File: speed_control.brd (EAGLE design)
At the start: 160 x 100 mm, 3 parts

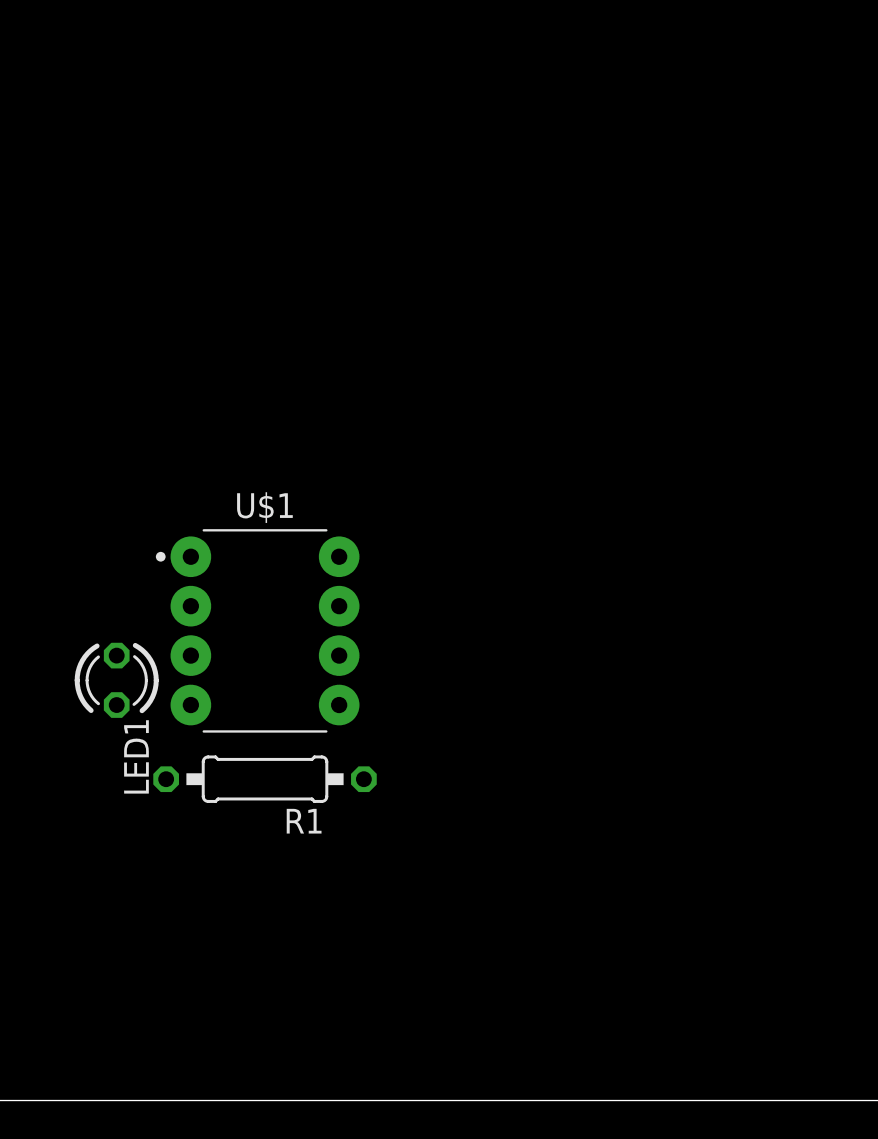
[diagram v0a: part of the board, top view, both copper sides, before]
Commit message: Added headers to circuit
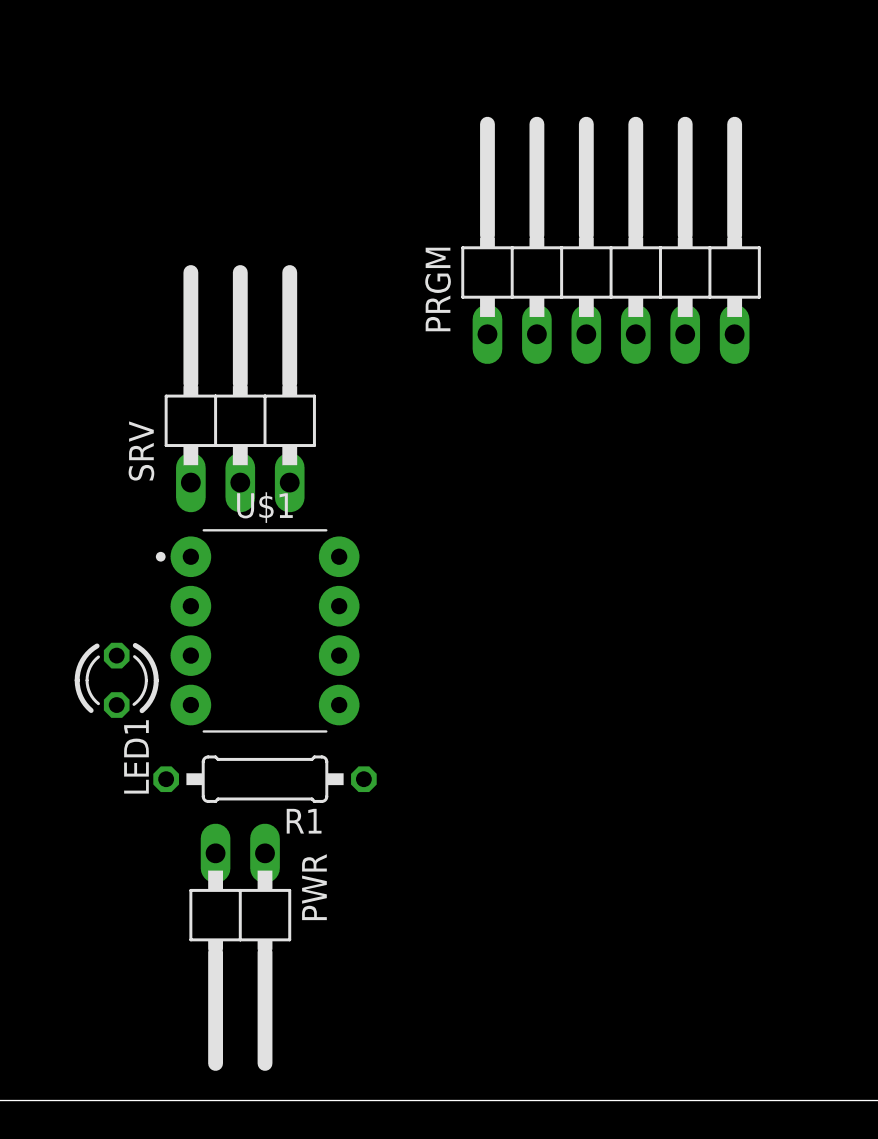
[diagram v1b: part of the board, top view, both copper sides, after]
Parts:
- added PRGM: (no value), pinhead:1X06/90
- added PWR: (no value), pinhead:1X02/90
- added SRV: (no value), pinhead:1X03/90
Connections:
- new net MCLR/VPP: PRGM.1
- new net PGC/ICSPCLK: PRGM.5
- new net PGD/ICSPDAT: PRGM.4
- new net PGM/LVP: PRGM.6
- new net VDD: PRGM.2
- new net VSS: PRGM.3
- net 5V: now also PWR.1, SRV.2
- net GND: now also PWR.2, SRV.1
- net SIGNAL: now also SRV.3
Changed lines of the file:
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@@
 </autorouter>
 <elements>
-<element name="U$1" library="PIC10F222" package="DIP762W53P254L955H330Q8B" package3d_urn="urn:adsk.eagle:package:16702925/1" value="PIC10F222PIC10F222" x="22.86" y="24.13" smashed="yes">
-<attribute name="NAME" x="22.86" y="29.9329" size="1.27" layer="25" align="bottom-center"/>
-<attribute name="VALUE" x="22.86" y="18.3271" size="1.27" layer="27" align="top-center"/>
-</element>
 <element name="LED1" library="led" library_urn="urn:adsk.eagle:library:259" package="LED3MM" package3d_urn="urn:adsk.eagle:package:15797/1" value="" x="15.24" y="21.59" smashed="yes" rot="R270">
 <attribute name="NAME" x="15.621" y="19.685" size="1.27" layer="25" ratio="10" rot="R270"/>
@@
 <attribute name="VALUE" x="25.1206" y="17.145" size="1.27" layer="27" ratio="10" rot="R180"/>
 </element>
+<element name="SRV" library="pinhead" library_urn="urn:adsk.eagle:library:325" package="1X03/90" package3d_urn="urn:adsk.eagle:package:22459/2" value="" x="21.59" y="35.56" smashed="yes">
+<attribute name="NAME" x="17.145" y="31.75" size="1.27" layer="25" ratio="10" rot="R90"/>
+<attribute name="POPULARITY" value="17" x="21.59" y="35.56" size="1.778" layer="27" display="off"/>
+<attribute name="VALUE" x="27.305" y="31.75" size="1.27" layer="27" rot="R90"/>
+</element>
+<element name="PWR" library="pinhead" library_urn="urn:adsk.eagle:library:325" package="1X02/90" package3d_urn="urn:adsk.eagle:package:22437/2" value="" x="21.59" y="8.89" smashed="yes" rot="R180">
+<attribute name="NAME" x="24.765" y="12.7" size="1.27" layer="25" ratio="10" rot="R270"/>
+<attribute name="POPULARITY" value="24" x="21.59" y="8.89" size="1.778" layer="27" rot="R180" display="off"/>
+<attribute name="VALUE" x="17.145" y="12.7" size="1.27" layer="27" rot="R270"/>
+</element>
+<element name="PRGM" library="pinhead" library_urn="urn:adsk.eagle:library:325" package="1X06/90" package3d_urn="urn:adsk.eagle:package:22475/2" value="" x="40.64" y="43.18" smashed="yes">
+<attribute name="NAME" x="32.385" y="39.37" size="1.27" layer="25" ratio="10" rot="R90"/>
+<attribute name="POPULARITY" value="10" x="40.64" y="43.18" size="1.778" layer="27" display="off"/>
+<attribute name="VALUE" x="50.165" y="39.37" size="1.27" layer="27" rot="R90"/>
+</element>
+<element name="U$1" library="PIC10F222" package="DIP762W53P254L955H330Q8B" package3d_urn="urn:adsk.eagle:package:16702925/1" value="PIC10F222PIC10F222" x="22.86" y="24.13" smashed="yes">
+<attribute name="NAME" x="22.86" y="29.9329" size="1.27" layer="25" align="bottom-center"/>
+<attribute name="VALUE" x="22.86" y="18.3271" size="1.27" layer="27" align="top-center"/>
+</element>
 </elements>
 <signals>
 <signal name="GND">
+<contactref element="R1" pad="1"/>
+<contactref element="PWR" pad="2"/>
+<contactref element="SRV" pad="1"/>
 <contactref element="U$1" pad="7"/>
-<contactref element="R1" pad="1"/>
-<wire x1="26.67" y1="25.4" x2="27.94" y2="16.51" width="0" layer="19" extent="1-1"/>
+<wire x1="27.94" y1="16.51" x2="26.67" y2="25.4" width="0" layer="19" extent="1-1"/>
+<wire x1="20.32" y1="12.7" x2="27.94" y2="16.51" width="0" layer="19" extent="1-1"/>
+<wire x1="19.05" y1="31.75" x2="26.67" y2="25.4" width="0" layer="19" extent="1-1"/>
 </signal>
 <signal name="5V">
+<contactref element="PWR" pad="1"/>
+<contactref element="SRV" pad="2"/>
 <contactref element="U$1" pad="2"/>
-</signal>
-<signal name="POT">
-<contactref element="U$1" pad="5"/>
+<wire x1="19.05" y1="25.4" x2="21.59" y2="31.75" width="0" layer="19" extent="1-1"/>
+<wire x1="22.86" y1="12.7" x2="19.05" y2="25.4" width="0" layer="19" extent="1-1"/>
 </signal>
 <signal name="SIGNAL">
+<contactref element="SRV" pad="3"/>
 <contactref element="U$1" pad="4"/>
+<wire x1="19.05" y1="20.32" x2="24.13" y2="31.75" width="0" layer="19" extent="1-1"/>
 </signal>
 <signal name="N$1">
+<contactref element="LED1" pad="A"/>
 <contactref element="U$1" pad="3"/>
-<contactref element="LED1" pad="A"/>
-<wire x1="19.05" y1="22.86" x2="15.24" y2="22.86" width="0" layer="19" extent="1-1"/>
+<wire x1="15.24" y1="22.86" x2="19.05" y2="22.86" width="0" layer="19" extent="1-1"/>
 </signal>
 <signal name="N$2">
@@
 <wire x1="17.78" y1="16.51" x2="15.24" y2="20.32" width="0" layer="19" extent="1-1"/>
 </signal>
+<signal name="MCLR/VPP">
+<contactref element="PRGM" pad="1"/>
+</signal>
+<signal name="VDD">
+<contactref element="PRGM" pad="2"/>
+</signal>
+<signal name="VSS">
+<contactref element="PRGM" pad="3"/>
+</signal>
+<signal name="PGD/ICSPDAT">
+<contactref element="PRGM" pad="4"/>
+</signal>
+<signal name="PGC/ICSPCLK">
+<contactref element="PRGM" pad="5"/>
+</signal>
+<signal name="PGM/LVP">
+<contactref element="PRGM" pad="6"/>
+</signal>
+<signal name="POT">
+<contactref element="U$1" pad="5"/>
+</signal>
 </signals>

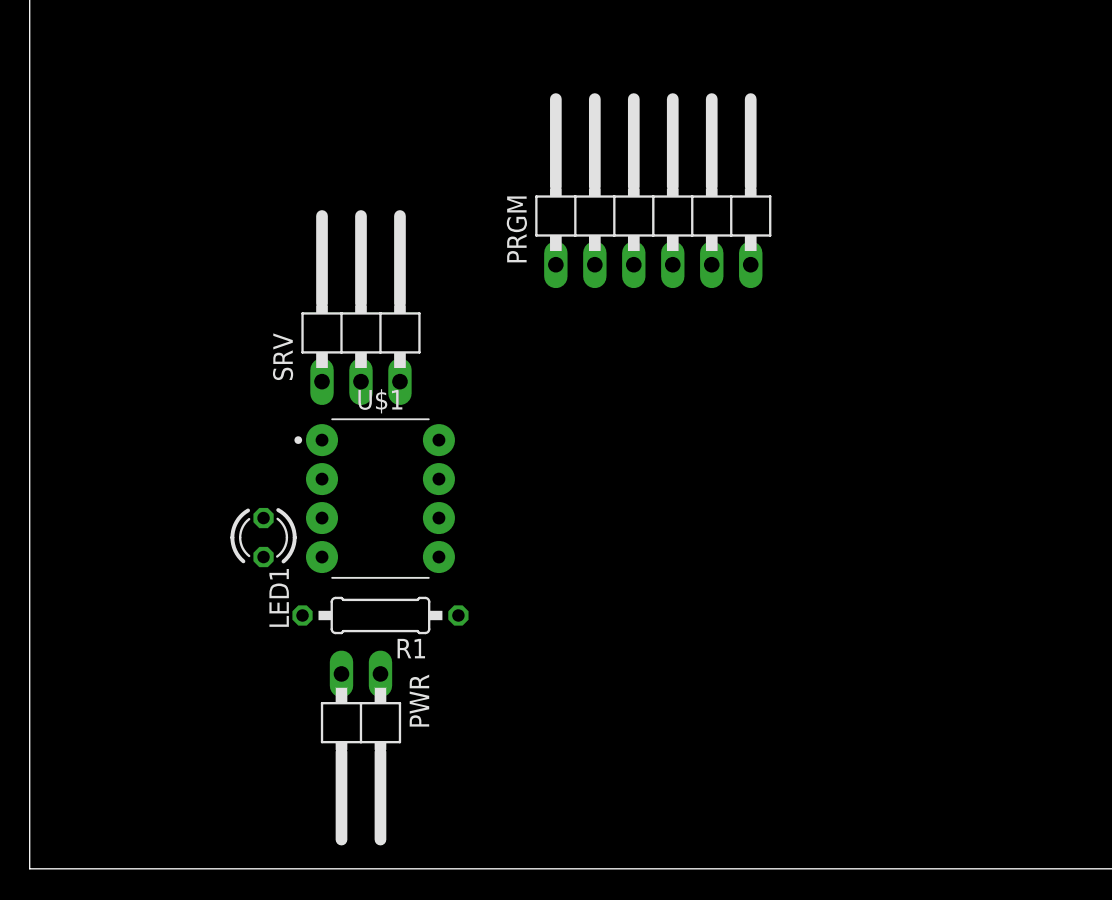
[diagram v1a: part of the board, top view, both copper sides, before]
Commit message: Added programming interface
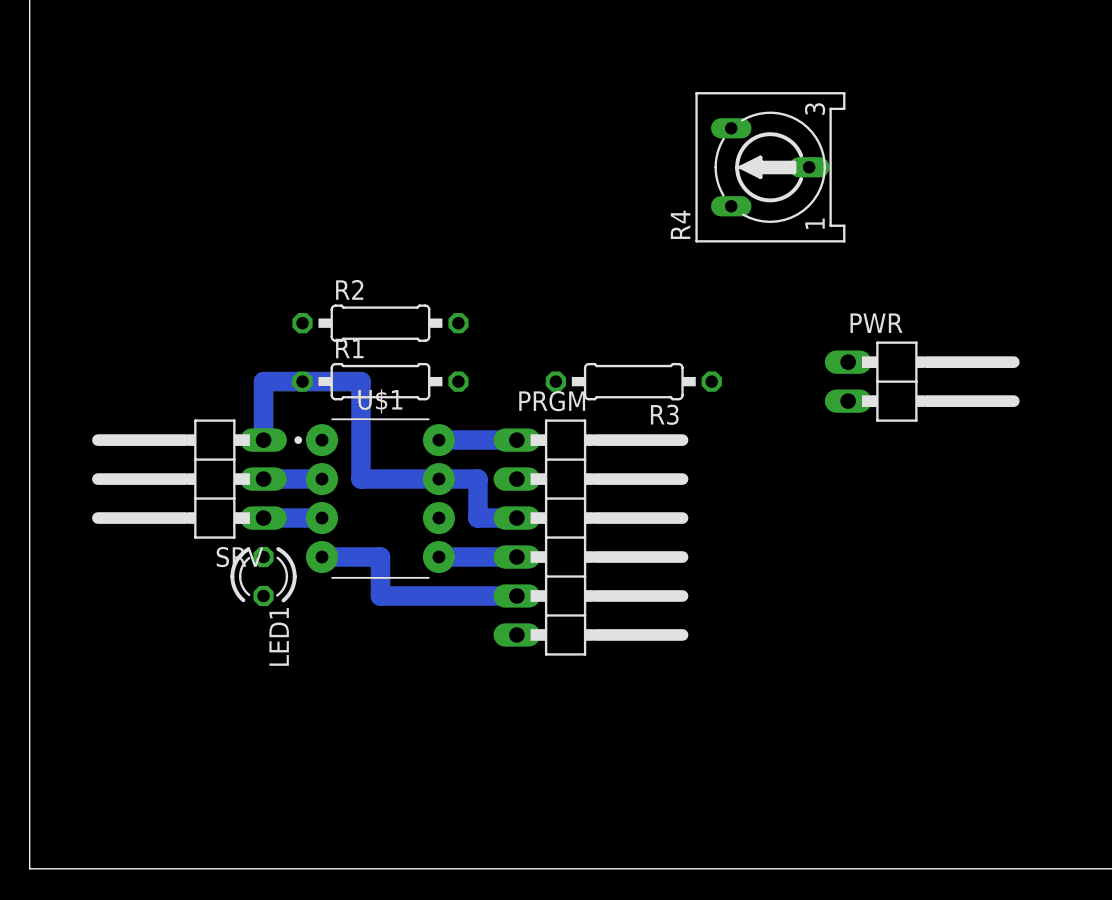
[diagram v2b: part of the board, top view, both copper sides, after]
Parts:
- added R2, R3: 1k, rcl:0207/10
- added R4: (no value), pot:RS3
- R1: value (none) -> 270
- moved PWR 42.3 mm to (57.1, 31.8), turned to 270 degrees
- moved PRGM 22.2 mm to (35.6, 21.6), turned to 270 degrees
- moved R1 15.2 mm to (22.9, 31.8), turned to 0 degrees
- moved SRV 14.4 mm to (11.4, 25.4), turned to 90 degrees
- moved LED1 2.54 mm to (15.2, 19.1)
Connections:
- removed net POT: U$1.5
- removed net VDD: PRGM.2
- removed net VSS: PRGM.3
- net 5V: now also PRGM.2, PWR.2, R2.1, R4.E; no longer PWR.1
- net GND: now also PRGM.3, PWR.1, R4.A, SRV.3; no longer PWR.2, SRV.1
- net MCLR/VPP: now also R2.2, U$1.8
- net N$1: now also R3.2, R4.S; no longer LED1.A, U$1.3
- net PGC/ICSPCLK: now also LED1.A, U$1.4
- net PGD/ICSPDAT: now also R3.1, U$1.5
- net SIGNAL: now also SRV.1, U$1.3; no longer SRV.3, U$1.4
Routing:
- net GND: track 0.00 -> 29.2 mm
- net PGC/ICSPCLK: track 0.00 -> 15.2 mm
- net PGD/ICSPDAT: track 0.00 -> 5.08 mm
- net MCLR/VPP: track 0.00 -> 5.08 mm
- net SIGNAL: track 0.00 -> 3.81 mm
- net 5V: track 0.00 -> 3.81 mm

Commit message: Layout of PCB complete
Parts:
- removed R4: (no value), pot:RS3
- added POT: (no value), pinhead:1X03
- PRGM: device pinhead:1X06/90 -> pinhead:1X06
- R2: value 1k -> 10k
- moved PWR 56.8 mm to (1.27, 21.6), turned to 90 degrees
- moved R3 26.9 mm to (20.3, 12.7), turned to 90 degrees
- moved R2 25.9 mm to (27.9, 10.2), turned to 90 degrees
- moved R1 24.4 mm to (7.62, 12.7), turned to 270 degrees
- moved PRGM 17.1 mm to (24.1, 8.89)
- moved LED1 16.5 mm to (8.89, 3.81), turned to 180 degrees
- moved SRV 16.3 mm to (1.27, 12.7)
- moved U$1 15.5 mm to (14.0, 11.4)
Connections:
- net 5V: now also POT.3; no longer R4.E
- net GND: now also POT.1; no longer R4.A
- net N$1: now also POT.2; no longer R4.S
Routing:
- net 5V: track 3.81 -> 109.8 mm
- net GND: track 29.2 -> 93.6 mm
- net PGC/ICSPCLK: track 15.2 -> 33.3 mm
- net MCLR/VPP: track 5.08 -> 10.2 mm
- net N$2: track 0.00 -> 3.81 mm
- net N$1: track 0.00 -> 2.54 mm
- net SIGNAL: track 3.81 -> 5.08 mm
- net PGD/ICSPDAT: track 5.08 -> 6.35 mm
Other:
- board size 160 x 100 mm -> 31.7 x 23.8 mm

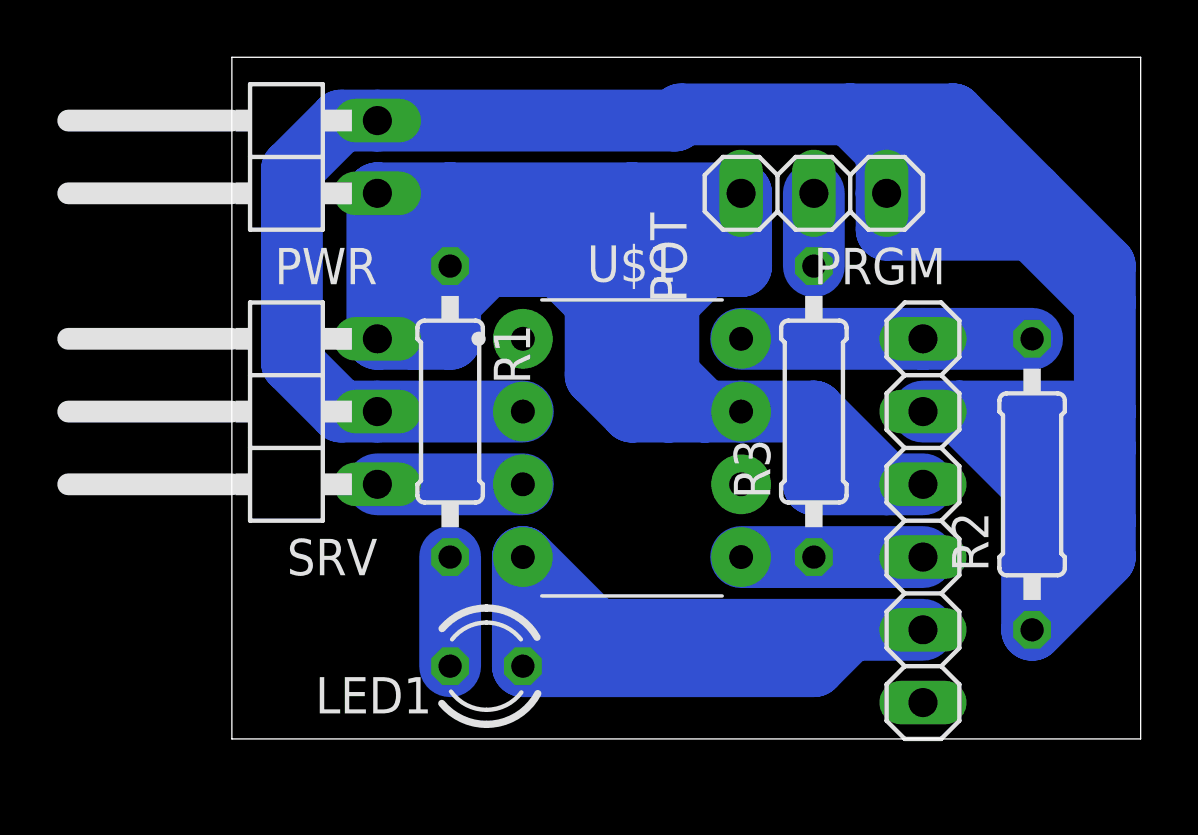
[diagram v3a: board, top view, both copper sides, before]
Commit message: Moved board to origin
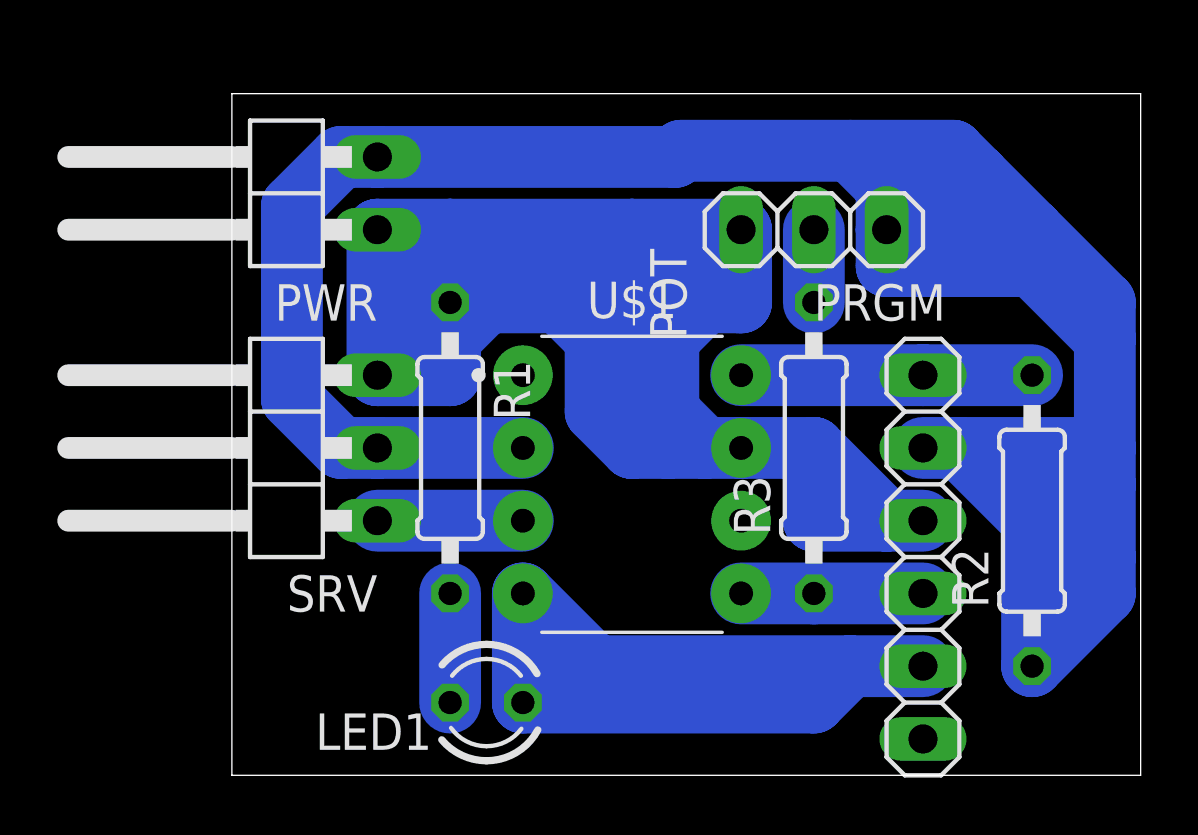
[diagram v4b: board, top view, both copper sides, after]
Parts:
- moved PRGM 1.27 mm to (24.1, 7.62)
- moved LED1 1.27 mm to (8.89, 2.54)
- moved POT 1.27 mm to (20.3, 19.1)
- moved PWR 1.27 mm to (1.27, 20.3)
- moved R1 1.27 mm to (7.62, 11.4)
- moved R2 1.27 mm to (27.9, 8.89)
- moved R3 1.27 mm to (20.3, 11.4)
- moved SRV 1.27 mm to (1.27, 11.4)
- moved U$1 1.27 mm to (14.0, 10.2)
